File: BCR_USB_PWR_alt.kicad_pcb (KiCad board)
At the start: 2 copper layers, 13.4 x 21.8 mm, 2 parts, among them CN1 DB9_Female, CN2 UE27AC54100

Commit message: clean up junk files
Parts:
- CN1: footprint 0_LOCAL:TE-5207826_nec -> 0_LOCAL:TE-5207826
- CN2: footprint 0_LOCAL:USB_A_Female_UE27AC54100_cut -> 0_LOCAL:USB_A_Female_UE27AC54100
- moved CN2 20.2 mm to (140.0, 95.8), turned to 270 degrees
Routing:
- net /GND: track 23.6 -> 12.2 mm
- net /+5V: track 18.9 -> 13.6 mm
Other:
- board size 13.4 x 21.8 mm -> 32.2 x 17 mm
- board text added: "5v USB power from BCR port"
- board text added: "TE 5207826"
- board text removed: "5v USB power"
- board text removed: "A-DF 09 PP/Z"
- board text removed: "NEC PC-8201 / PC-8300"
- board text removed: "from BCR port"

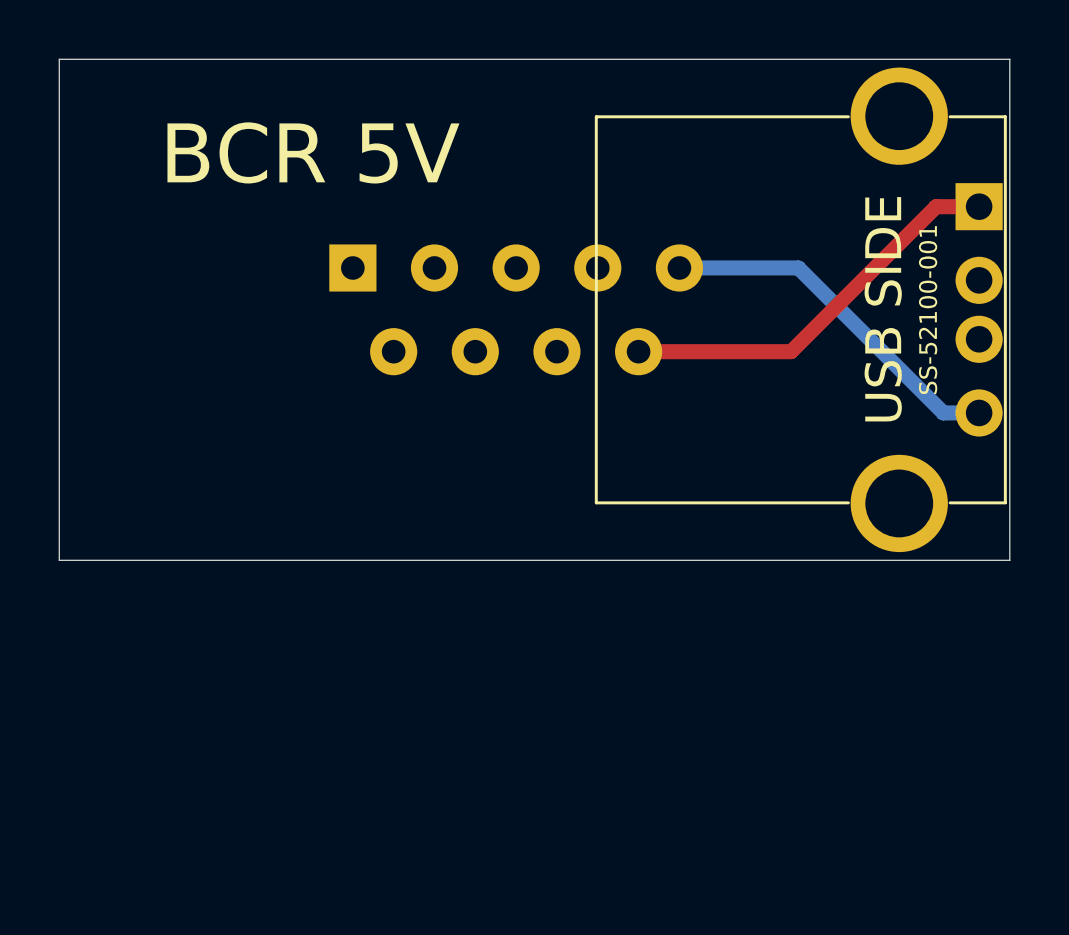
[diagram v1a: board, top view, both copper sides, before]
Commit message: rename NEC to up_long, and a short up version that covers up the shorting hazard
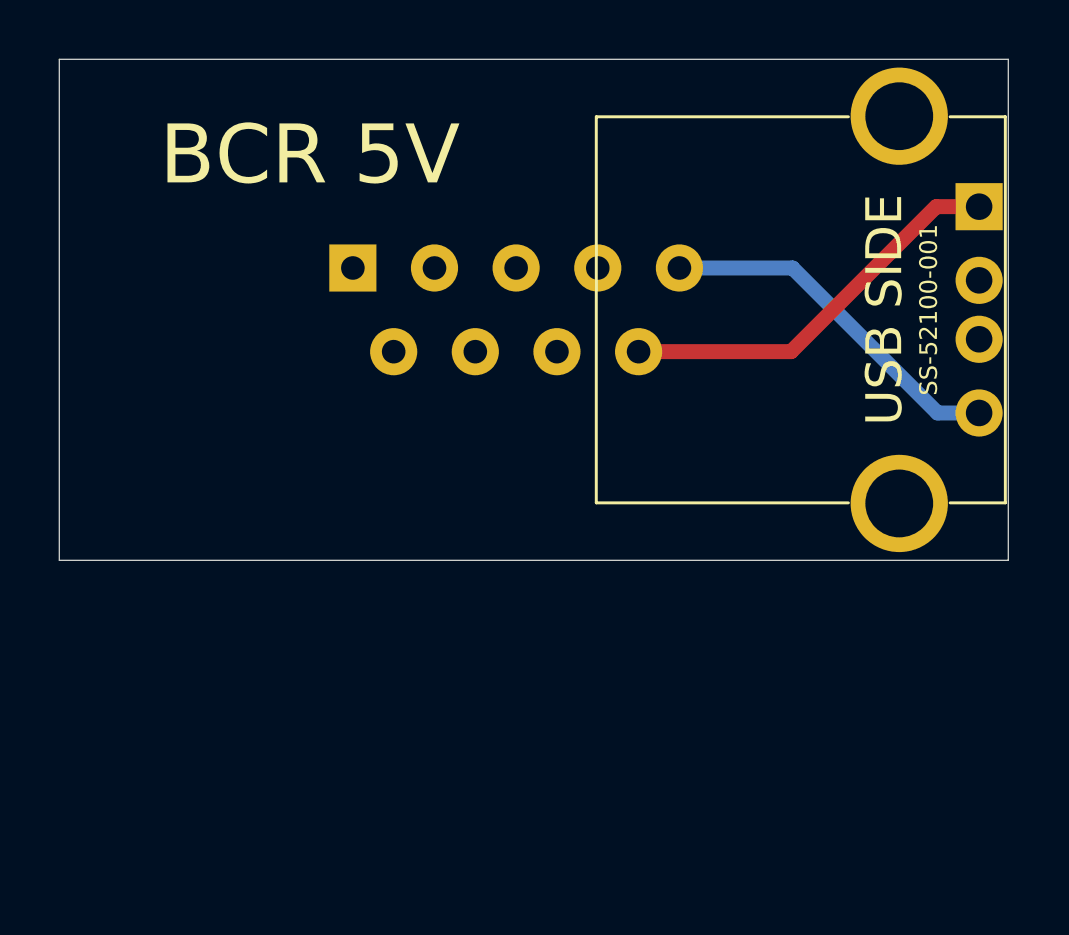
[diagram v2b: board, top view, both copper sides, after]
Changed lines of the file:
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@@
   )
   (gr_line (start 111.5 87.258) (end 111.5 104.258) (layer Edge.Cuts) (width 0.0254))
-  (gr_line (start 143.75 87.258) (end 111.5 87.258) (layer Edge.Cuts) (width 0.0254))
-  (gr_line (start 143.75 104.258) (end 143.75 87.258) (layer Edge.Cuts) (width 0.0254))
-  (gr_line (start 111.5 104.258) (end 143.75 104.258) (layer Edge.Cuts) (width 0.0254))
+  (gr_line (start 143.7 87.258) (end 111.5 87.258) (layer Edge.Cuts) (width 0.0254))
+  (gr_line (start 143.7 104.258) (end 143.7 87.258) (layer Edge.Cuts) (width 0.0254))
+  (gr_line (start 111.5 104.258) (end 143.7 104.258) (layer Edge.Cuts) (width 0.0254))
   (segment (start 141.25 92.258) (end 142.71 92.258) (width 0.508) (layer F.Cu) (net 1))
   (segment (start 131.15526 97.17814) (end 136.32986 97.17814) (width 0.508) (layer F.Cu) (net 1))
   (segment (start 136.32986 97.17814) (end 141.25 92.258) (width 0.508) (layer F.Cu) (net 1))
-  (segment (start 142.71 99.258) (end 141.5 99.258) (width 0.508) (layer B.Cu) (net 2))
-  (segment (start 136.58014 94.33814) (end 132.54026 94.33814) (width 0.508) (layer B.Cu) (net 2))
-  (segment (start 141.5 99.258) (end 136.58014 94.33814) (width 0.508) (layer B.Cu) (net 2))
+  (segment (start 136.38014 94.33814) (end 132.54026 94.33814) (width 0.508) (layer B.Cu) (net 2))
+  (segment (start 142.71 99.258) (end 141.3 99.258) (width 0.508) (layer B.Cu) (net 2))
+  (segment (start 141.3 99.258) (end 136.38014 94.33814) (width 0.508) (layer B.Cu) (net 2))
 )

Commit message: Add BCR_Breakout. Rename repo to BCR_Breakout.
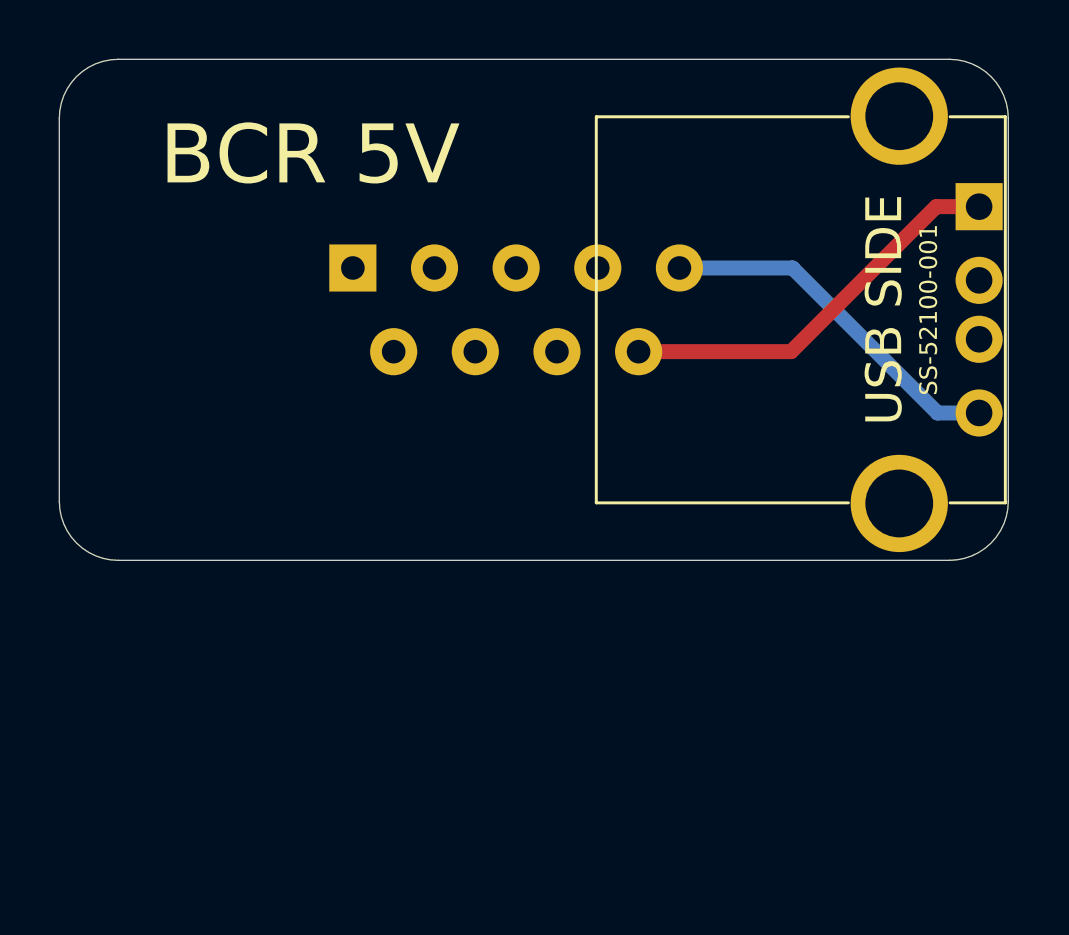
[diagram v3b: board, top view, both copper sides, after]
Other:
- outline, holes or cut-outs redrawn
- board text added: "github.com/bkw777/BCR_Breakout"
- board text removed: "github.com/bkw777/BCR_USB_PWR"
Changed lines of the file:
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@@
   (general
     (thickness 1.6)
-    (drawings 13)
+    (drawings 17)
     (tracks 6)
     (zones 0)
@@
     (uvia_min_size 0.2)
     (uvia_min_drill 0.1)
-    (edge_width 0.05)
+    (edge_width 0.025)
     (segment_width 0.2)
     (pcb_text_width 0.3)
@@
     (add_net "Net-(CN2-PadSH)")
   )
-  (module 0_LOCAL:USB_A_Female_UE27AC54100 (layer F.Cu)
-    (at 140 95.758 270)
-    (fp_text reference CN2 (at 0 -0.889 270 unlocked) (layer F.SilkS) hide
-      (effects (font (size 1 1) (thickness 0.15)))
-    )
-    (fp_text value UE27AC54100 (at 0 9.4 270) (layer F.Fab)
-      (effects (font (size 1 1) (thickness 0.15)))
-    )
-    (fp_line (start -6.55 -3.6) (end 6.55 -3.6) (layer F.SilkS) (width 0.1))
-    (fp_line (start 6.55 1.725) (end 6.55 10.28) (layer F.SilkS) (width 0.1))
-    (fp_line (start -6.55 1.725) (end -6.55 10.28) (layer F.SilkS) (width 0.1))
-    (fp_line (start -6.55 -3.6) (end -6.55 -1.725) (layer F.SilkS) (width 0.1))
-    (fp_line (start -6.55 -3.6) (end 6.55 -3.6) (layer F.Fab) (width 0.1))
-    (fp_line (start 6.55 -3.6) (end 6.55 10.28) (layer F.Fab) (width 0.1))
-    (fp_line (start -6.55 -3.6) (end -6.55 10.28) (layer F.Fab) (width 0.1))
-    (fp_line (start -6.55 10.28) (end 6.55 10.28) (layer F.Fab) (width 0.1))
-    (fp_line (start 6.55 -3.6) (end 6.55 -1.725) (layer F.SilkS) (width 0.1))
-    (fp_line (start 6.55 10.28) (end -6.55 10.28) (layer F.SilkS) (width 0.1))
-    (fp_line (start -8.45 -3.94) (end 8.45 -3.94) (layer F.CrtYd) (width 0.05))
-    (fp_line (start 8.45 -3.94) (end 8.45 10.375) (layer F.CrtYd) (width 0.05))
-    (fp_line (start -8.45 -3.94) (end -8.45 10.375) (layer F.CrtYd) (width 0.05))
-    (fp_line (start -8.45 10.375) (end 8.45 10.375) (layer F.CrtYd) (width 0.05))
-    (fp_text user %R (at -0.025 0.975 270) (layer F.Fab)
-      (effects (font (size 1 1) (thickness 0.15)))
-    )
-    (pad 4 thru_hole circle (at 3.5 -2.71 270) (size 1.6 1.6) (drill 0.9) (layers *.Cu *.Mask)
-      (net 2 /GND))
-    (pad 3 thru_hole circle (at 1 -2.71 270) (size 1.6 1.6) (drill 0.9) (layers *.Cu *.Mask))
-    (pad 2 thru_hole circle (at -1 -2.71 270) (size 1.6 1.6) (drill 0.9) (layers *.Cu *.Mask))
-    (pad 1 thru_hole rect (at -3.5 -2.71 270) (size 1.6 1.6) (drill 0.9) (layers *.Cu *.Mask)
-      (net 1 /+5V))
-    (pad SH thru_hole circle (at 6.57 0 270) (size 3.3 3.3) (drill 2.3) (layers *.Cu *.Mask)
-      (net 3 "Net-(CN2-PadSH)"))
-    (pad SH thru_hole circle (at -6.57 0 270) (size 3.3 3.3) (drill 2.3) (layers *.Cu *.Mask)
-      (net 3 "Net-(CN2-PadSH)"))
-    (model ${KIPRJMOD}/3dmodels/USB-A_female_horiz_thru.step
-      (offset (xyz 0 3.5 6.9))
-      (scale (xyz 1 1 1))
-      (rotate (xyz 0 0 0))
-    )
-  )
   (module 0_LOCAL:TE-5207826 (layer B.Cu)
     (at 121.46026 94.33814 180)
@@
     )
   )
+  (module 0_LOCAL:USB_A_Female_UE27AC54100 (layer F.Cu)
+    (at 140 95.758 270)
+    (fp_text reference CN2 (at 0 -0.889 270 unlocked) (layer F.SilkS) hide
+      (effects (font (size 1 1) (thickness 0.15)))
+    )
+    (fp_text value UE27AC54100 (at 0 9.4 270) (layer F.Fab)
+      (effects (font (size 1 1) (thickness 0.15)))
+    )
+    (fp_line (start -6.55 -3.6) (end 6.55 -3.6) (layer F.SilkS) (width 0.1))
+    (fp_line (start 6.55 1.725) (end 6.55 10.28) (layer F.SilkS) (width 0.1))
+    (fp_line (start -6.55 1.725) (end -6.55 10.28) (layer F.SilkS) (width 0.1))
+    (fp_line (start -6.55 -3.6) (end -6.55 -1.725) (layer F.SilkS) (width 0.1))
+    (fp_line (start -6.55 -3.6) (end 6.55 -3.6) (layer F.Fab) (width 0.1))
+    (fp_line (start 6.55 -3.6) (end 6.55 10.28) (layer F.Fab) (width 0.1))
+    (fp_line (start -6.55 -3.6) (end -6.55 10.28) (layer F.Fab) (width 0.1))
+    (fp_line (start -6.55 10.28) (end 6.55 10.28) (layer F.Fab) (width 0.1))
+    (fp_line (start 6.55 -3.6) (end 6.55 -1.725) (layer F.SilkS) (width 0.1))
+    (fp_line (start 6.55 10.28) (end -6.55 10.28) (layer F.SilkS) (width 0.1))
+    (fp_line (start -8.45 -3.94) (end 8.45 -3.94) (layer F.CrtYd) (width 0.05))
+    (fp_line (start 8.45 -3.94) (end 8.45 10.375) (layer F.CrtYd) (width 0.05))
+    (fp_line (start -8.45 -3.94) (end -8.45 10.375) (layer F.CrtYd) (width 0.05))
+    (fp_line (start -8.45 10.375) (end 8.45 10.375) (layer F.CrtYd) (width 0.05))
+    (fp_text user %R (at -0.025 0.975 270) (layer F.Fab)
+      (effects (font (size 1 1) (thickness 0.15)))
+    )
+    (pad 4 thru_hole circle (at 3.5 -2.71 270) (size 1.6 1.6) (drill 0.9) (layers *.Cu *.Mask)
+      (net 2 /GND))
+    (pad 3 thru_hole circle (at 1 -2.71 270) (size 1.6 1.6) (drill 0.9) (layers *.Cu *.Mask))
+    (pad 2 thru_hole circle (at -1 -2.71 270) (size 1.6 1.6) (drill 0.9) (layers *.Cu *.Mask))
+    (pad 1 thru_hole rect (at -3.5 -2.71 270) (size 1.6 1.6) (drill 0.9) (layers *.Cu *.Mask)
+      (net 1 /+5V))
+    (pad SH thru_hole circle (at 6.57 0 270) (size 3.3 3.3) (drill 2.3) (layers *.Cu *.Mask)
+      (net 3 "Net-(CN2-PadSH)"))
+    (pad SH thru_hole circle (at -6.57 0 270) (size 3.3 3.3) (drill 2.3) (layers *.Cu *.Mask)
+      (net 3 "Net-(CN2-PadSH)"))
+    (model ${KIPRJMOD}/3dmodels/USB-A_female_horiz_thru.step
+      (offset (xyz 0 3.5 6.9))
+      (scale (xyz 1 1 1))
+      (rotate (xyz 0 0 0))
+    )
+  )
+  (gr_arc (start 141.7 102.258) (end 141.7 104.258) (angle -90) (layer Edge.Cuts) (width 0.025))
+  (gr_arc (start 141.7 89.258) (end 143.7 89.258) (angle -90) (layer Edge.Cuts) (width 0.025))
+  (gr_arc (start 113.5 89.258) (end 113.5 87.258) (angle -90) (layer Edge.Cuts) (width 0.025))
+  (gr_arc (start 113.5 102.258) (end 111.5 102.258) (angle -90) (layer Edge.Cuts) (width 0.025))
+  (gr_line (start 111.5 89.258) (end 111.5 102.258) (layer Edge.Cuts) (width 0.025))
+  (gr_line (start 141.7 87.258) (end 113.5 87.258) (layer Edge.Cuts) (width 0.025))
+  (gr_line (start 143.7 102.258) (end 143.7 89.258) (layer Edge.Cuts) (width 0.025))
+  (gr_line (start 113.5 104.258) (end 141.7 104.258) (layer Edge.Cuts) (width 0.025))
   (gr_text "TE 5207826" (at 127 99.008) (layer B.SilkS)
     (effects (font (size 0.6 0.6) (thickness 0.1)) (justify mirror))
@@
     (effects (font (size 0.6 0.6) (thickness 0.1)))
   )
-  (gr_text github.com/bkw777/BCR_USB_PWR (at 127 103.258) (layer B.SilkS)
+  (gr_text github.com/bkw777/BCR_Breakout (at 127 103.258) (layer B.SilkS)
     (effects (font (size 0.6 0.6) (thickness 0.1)) (justify mirror))
   )
@@
     (effects (font (size 1.2192 1.2192) (thickness 0.2032)))
   )
-  (gr_line (start 111.5 87.258) (end 111.5 104.258) (layer Edge.Cuts) (width 0.0254))
-  (gr_line (start 143.7 87.258) (end 111.5 87.258) (layer Edge.Cuts) (width 0.0254))
-  (gr_line (start 143.7 104.258) (end 143.7 87.258) (layer Edge.Cuts) (width 0.0254))
-  (gr_line (start 111.5 104.258) (end 143.7 104.258) (layer Edge.Cuts) (width 0.0254))
   (segment (start 141.25 92.258) (end 142.71 92.258) (width 0.508) (layer F.Cu) (net 1))
   (segment (start 131.15526 97.17814) (end 136.32986 97.17814) (width 0.508) (layer F.Cu) (net 1))

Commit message: change metal db9 to plastic
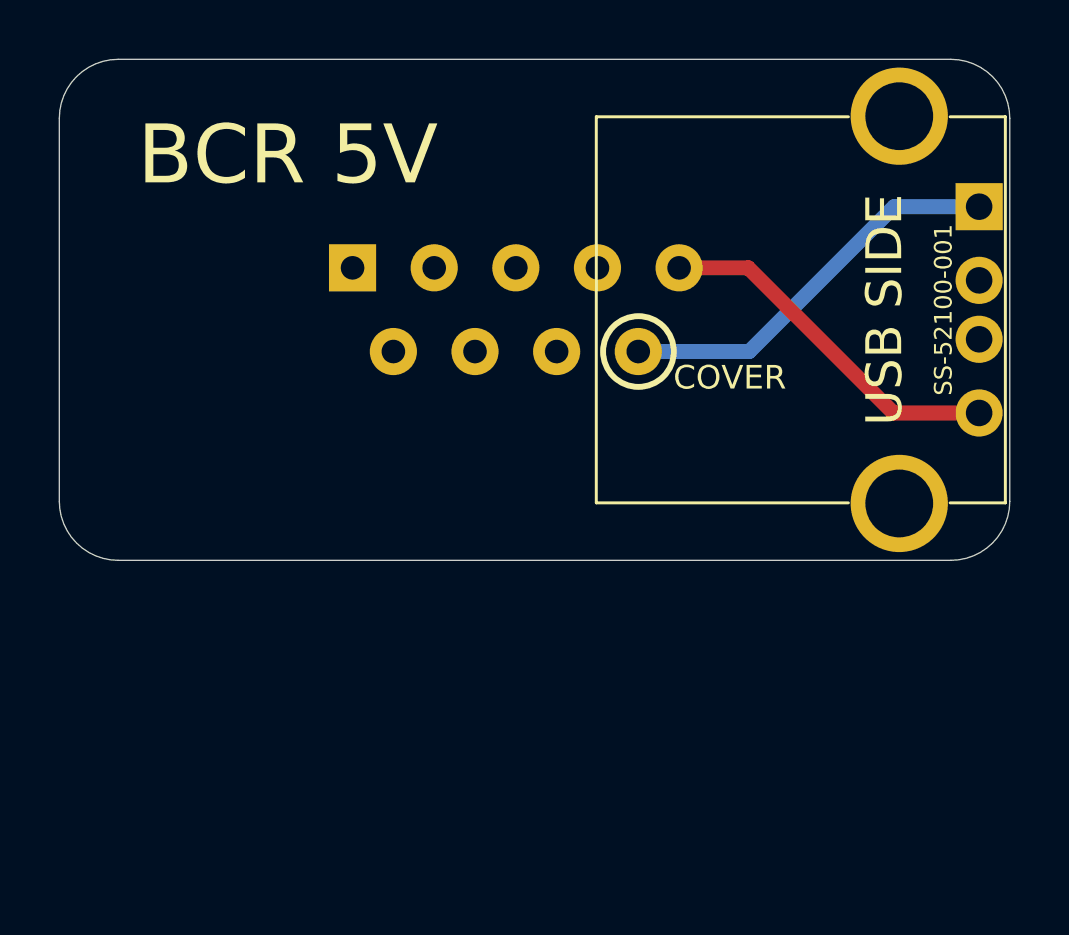
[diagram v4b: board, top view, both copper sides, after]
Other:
- board text added: "COVER"
